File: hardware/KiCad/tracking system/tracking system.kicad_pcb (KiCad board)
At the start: 2 copper layers, 60 x 40 mm, 47 parts, among them J1 TP_SWD, J2 USB_C_Receptacle_PowerOnly_6P, J3 battery_conn, J5 GPS_Conn, J6 GSM_Conn, J7 OLED_conn, SW1 POWER_BTN, SW2 DIST_BTN, U1 STM32L476RETx, U2 TP4056-42-ESOP8, U3 ME6211C33M5, Y1 32kHz, Y2 8MHz

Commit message: work in progress
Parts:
- moved R7 79.8 mm to (129.0, 106.2)
- moved R8 79.6 mm to (129.0, 112.7)
- moved D1 63.4 mm to (154.5, 97.2), turned to 180 degrees
- moved C18 60.9 mm to (157.0, 112.0)
- moved C17 59.2 mm to (157.8, 107.0), turned to 180 degrees
- moved C19 57.7 mm to (159.7, 112.0), turned to 180 degrees
- moved R6 57.5 mm to (149.8, 102.8), turned to -90 degrees
- moved R5 50.6 mm to (158.0, 97.2)
- moved R9 49.5 mm to (160.5, 104.5), turned to -90 degrees
- moved C16 47.9 mm to (151.5, 107.0), turned to 180 degrees
- moved R4 44.3 mm to (163.0, 100.5), turned to -90 degrees
- moved R3 43.7 mm to (163.0, 98.2), turned to -90 degrees
- moved U2 3.26 mm to (155.2, 102.5)
- moved SW1 1.32 mm to (124.2, 107.2)
- moved SW2 1.32 mm to (124.2, 113.5)
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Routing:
- net +3.3V: track 0.00 -> 89.7 mm, vias 0 -> 2
- net GND: track 0.00 -> 78.5 mm, vias 0 -> 9
- net BTN_INT_EX2: track 0.00 -> 31.2 mm, vias 0 -> 4
- net BTN_PWR_EX3: track 0.00 -> 21.3 mm, vias 0 -> 2
- net RCC_OSC32_OUT: track 0.00 -> 19.2 mm, vias 0 -> 2
- net RCC_OSC_IN: track 0.00 -> 18.1 mm
- net RCC_OSC32_IN: track 0.00 -> 16.5 mm
- net USART3_RX: track 0.00 -> 14.5 mm
- net USART3_TX: track 0.00 -> 14.0 mm
- net /SWDIO: track 0.00 -> 12.8 mm
- net RCC_OSC_OUT: track 0.00 -> 12.2 mm
- net +3.3VA: track 0.00 -> 10.8 mm
- net /SWCLK: track 0.00 -> 7.93 mm
- net Net-(C12-Pad1): track 0.00 -> 4.70 mm
- net /NRST: track 0.00 -> 3.98 mm
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- added copper zone on F.Cu, net (none)
- added copper zone on B.Cu, net GND

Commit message: final pcb design
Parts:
- moved C3 1.75 mm to (135.5, 89.8)
- moved R2 1.75 mm to (137.8, 89.8)
- moved D1 0.25 mm to (154.8, 97.2)
- turned R5 to 180 degrees
- turned R6 to 90 degrees
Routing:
- net VBAT: track 0.00 -> 119.0 mm, vias 0 -> 6
- net +3.3V: track 89.7 -> 159.0 mm, vias 2 -> 4
- net GND: track 78.5 -> 126.4 mm, vias 9 -> 11
- net VBUS: track 0.00 -> 40.5 mm, vias 0 -> 2
- net USART1_TX: track 0.00 -> 22.5 mm
- net USART1_RX: track 0.00 -> 18.8 mm
- net I2C1_SDA: track 0.00 -> 14.5 mm
- net I2C1_SCL: track 0.00 -> 13.8 mm
- net Net-(U2-~{CHRG}): track 0.00 -> 6.99 mm, vias 0 -> 2
- net Net-(J2-CC1): track 0.00 -> 4.02 mm
- net Net-(J2-CC2): track 0.00 -> 3.92 mm
- net Net-(U2-PROG): track 0.00 -> 3.60 mm
- net Net-(U2-~{STDBY}): track 0.00 -> 3.13 mm
- net Net-(D1-K): track 0.00 -> 1.95 mm
- net /BOOT0: track 2.42 -> 3.54 mm
- removed copper zone on F.Cu, net (none)

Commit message: PCB done. About to send the files and start the firmware
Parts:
- added G***: LOGO, LOGO, F.Cu at (167.0, 90.2)
- moved H2 0.35 mm to (170.1, 117.4)
- moved H4 0.35 mm to (116.9, 117.4)
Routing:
- net GND: track 126.4 -> 127.9 mm, vias 11 -> 12
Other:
- outline, holes or cut-outs redrawn
- board text added: "MB-TRACK V1"

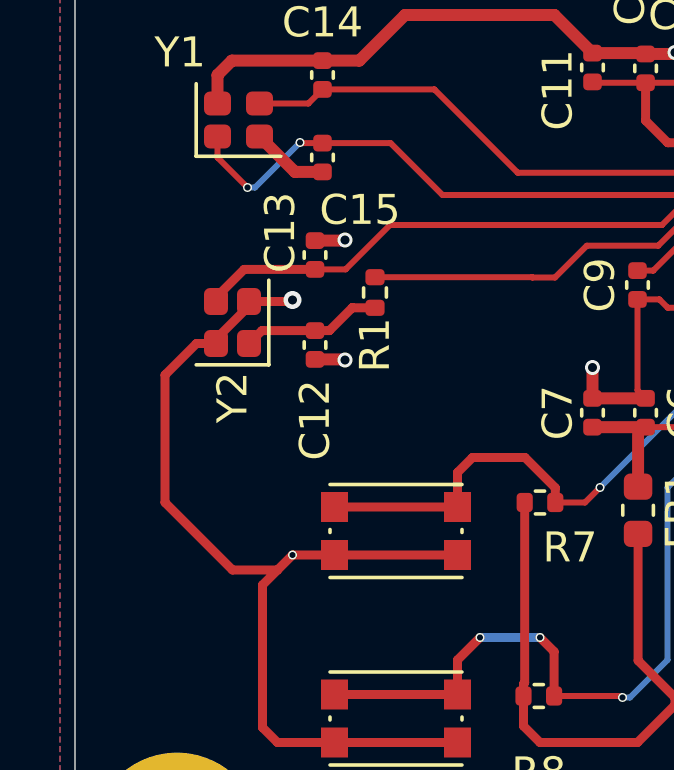
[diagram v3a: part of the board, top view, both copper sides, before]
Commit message: making changes to schematics and updating pcb
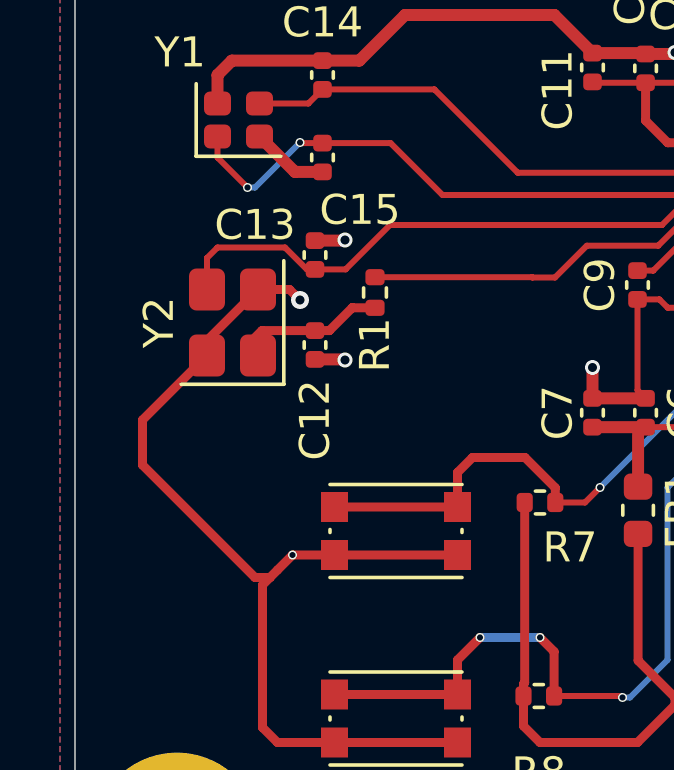
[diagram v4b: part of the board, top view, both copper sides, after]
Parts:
- Y2: footprint Crystal:Crystal_SMD_2016-4Pin_2.0x1.6mm -> Crystal:Crystal_SMD_3225-4Pin_3.2x2.5mm
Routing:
- net RCC_OSC_IN: track 18.1 -> 19.5 mm
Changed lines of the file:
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@@
 		(embedded_fonts no)
 	)
-	(footprint "Crystal:Crystal_SMD_2016-4Pin_2.0x1.6mm"
+	(footprint "Crystal:Crystal_SMD_3225-4Pin_3.2x2.5mm"
 		(layer "F.Cu")
 		(at 118.75 100.25 90)
-		(descr "SMD2016/4, Crystal, 2.0x1.6mm package, SMD, http://www.q-crystal.com/upload/5/2015552223166229.pdf")
+		(descr "SMD3225/4, Crystal, 3.2x2.5mm package, SMD, http://www.txccrystal.com/images/pdf/7m-accuracy.pdf")
 		(property "Reference" "Y2"
-			(at -2.5 0 90)
+			(at 0 -2.45 90)
 			(layer "F.SilkS")
 			(effects
@@
 		)
 		(property "Value" "8MHz"
-			(at 0 2 90)
+			(at 3 -3 90)
 			(layer "F.Fab")
 			(hide yes)
@@
 		(duplicate_pad_numbers_are_jumpers no)
 		(fp_line
-			(start -1.41 -1.21)
-			(end -1.41 1.21)
+			(start -2.06 -1.71)
+			(end -2.06 1.71)
 			(stroke
 				(width 0.12)
@@
 		)
 		(fp_line
-			(start -1.41 1.21)
-			(end 1.41 1.21)
+			(start -2.06 1.71)
+			(end 2.06 1.71)
 			(stroke
 				(width 0.12)
@@
 		)
 		(fp_rect
-			(start -1.5 -1.3)
-			(end 1.5 1.3)
+			(start -2.1 -1.75)
+			(end 2.1 1.75)
 			(stroke
 				(width 0.05)
@@
 		(fp_poly
 			(pts
-				(xy 1 -0.8) (xy 1 0.8) (xy -0.6 0.8) (xy -1 0.4) (xy -1 -0.8)
+				(xy 1.6 -1.25) (xy 1.6 1.25) (xy -0.975 1.25) (xy -1.6 0.625) (xy -1.6 -1.25)
 			)
 			(stroke
@@
 		)
 		(pad "1" smd roundrect
-			(at -0.7 0.55 90)
-			(size 0.9 0.8)
+			(at -1.1 0.85 90)
+			(size 1.4 1.2)
 			(layers "F.Cu" "F.Mask" "F.Paste")
-			(roundrect_rratio 0.25)
+			(roundrect_rratio 0.208333)
 			(net "Net-(C12-Pad1)")
 			(pinfunction "1_1")
@@
 		)
 		(pad "2" smd roundrect
-			(at 0.7 0.55 90)
-			(size 0.9 0.8)
+			(at 1.1 0.85 90)
+			(size 1.4 1.2)
 			(layers "F.Cu" "F.Mask" "F.Paste")
-			(roundrect_rratio 0.25)
+			(roundrect_rratio 0.208333)
 			(net "GND")
 			(pinfunction "G_2")
@@
 		)
 		(pad "3" smd roundrect
-			(at 0.7 -0.55 90)
-			(size 0.9 0.8)
+			(at 1.1 -0.85 90)
+			(size 1.4 1.2)
 			(layers "F.Cu" "F.Mask" "F.Paste")
-			(roundrect_rratio 0.25)
+			(roundrect_rratio 0.208333)
 			(net "RCC_OSC_IN")
 			(pinfunction "3_3")
@@
 		)
 		(pad "4" smd roundrect
-			(at -0.7 -0.55 90)
-			(size 0.9 0.8)
+			(at -1.1 -0.85 90)
+			(size 1.4 1.2)
 			(layers "F.Cu" "F.Mask" "F.Paste")
-			(roundrect_rratio 0.25)
+			(roundrect_rratio 0.208333)
 			(net "GND")
 			(pinfunction "G_4")
@@
 		)
 		(embedded_fonts no)
-		(model "${KICAD10_3DMODEL_DIR}/Crystal.3dshapes/Crystal_SMD_2016-4Pin_2.0x1.6mm.step"
+		(model "${KICAD10_3DMODEL_DIR}/Crystal.3dshapes/Crystal_SMD_3225-4Pin_3.2x2.5mm.step"
 			(offset
 				(xyz 0 0 0)
@@
 		(tags "capacitor")
 		(property "Reference" "C13"
-			(at 0.75 -1.16 90)
+			(at 1 -2 180)
 			(layer "F.SilkS")
 			(effects
@@
 	)
 	(segment
-		(start 147.319584 95.005575)
-		(end 147.336464 94.988695)
+		(start 115.75 103.5)
+		(end 115.75 105)
 		(width 0.3)
 		(layer "F.Cu")
@@
 	)
 	(segment
-		(start 119.3 99.55)
-		(end 119.3 99.7)
+		(start 147.319584 95.005575)
+		(end 147.336464 94.988695)
 		(width 0.3)
 		(layer "F.Cu")
@@
 	)
 	(segment
+		(start 119.5 108.75)
+		(end 120 108.75)
+		(width 0.3)
+		(layer "F.Cu")
+		(net "GND")
+	)
+	(segment
 		(start 137.269584 92.333695)
 		(end 137.269584 93.269584)
@@
 	)
 	(segment
-		(start 116.5 106.25)
-		(end 118.75 108.5)
-		(width 0.3)
-		(layer "F.Cu")
-		(net "GND")
-	)
-	(segment
 		(start 133.258695 99.758695)
 		(end 132.98 99.48)
@@
 	)
 	(segment
-		(start 119.3 99.55)
-		(end 120.7 99.55)
-		(width 0.3)
-		(layer "F.Cu")
-		(net "GND")
-	)
-	(segment
 		(start 142.75 111.5)
 		(end 143 111.75)
@@
 	)
 	(segment
-		(start 119.75 109)
+		(start 120 108.75)
 		(end 120.25 108.5)
 		(width 0.3)
@@
 	)
 	(segment
-		(start 119.3 99.7)
-		(end 118.2 100.8)
-		(width 0.3)
-		(layer "F.Cu")
-		(net "GND")
-	)
-	(segment
 		(start 164.25 102)
 		(end 166.92 102)
@@
 	)
 	(segment
-		(start 116.5 102)
-		(end 116.5 106.25)
+		(start 121.5 97.52)
+		(end 122.48 97.52)
+		(width 0.4)
+		(layer "F.Cu")
+		(net "GND")
+	)
+	(segment
+		(start 122.15 114.25)
+		(end 120.25 114.25)
 		(width 0.3)
 		(layer "F.Cu")
@@
 	)
 	(segment
-		(start 121.5 97.52)
-		(end 122.48 97.52)
+		(start 130.75 102.778695)
+		(end 130.75 101.75)
 		(width 0.4)
 		(layer "F.Cu")
@@
 	)
 	(segment
-		(start 118.2 100.95)
-		(end 117.55 100.95)
+		(start 119.6 99.15)
+		(end 120.65 99.15)
 		(width 0.3)
 		(layer "F.Cu")
@@
 	)
 	(segment
-		(start 122.15 114.25)
-		(end 120.25 114.25)
+		(start 119.75 109)
+		(end 120 108.75)
 		(width 0.3)
 		(layer "F.Cu")
@@
 	)
 	(segment
-		(start 130.75 102.778695)
-		(end 130.75 101.75)
-		(width 0.4)
+		(start 117.9 101.35)
+		(end 117.9 100.85)
+		(width 0.3)
+		(layer "F.Cu")
+		(net "GND")
+	)
+	(segment
+		(start 120.65 99.15)
+		(end 121 99.5)
+		(width 0.3)
 		(layer "F.Cu")
 		(net "GND")
@@
 	)
 	(segment
+		(start 117.9 101.35)
+		(end 115.75 103.5)
+		(width 0.3)
+		(layer "F.Cu")
+		(net "GND")
+	)
+	(segment
 		(start 120.25 108.5)
 		(end 120.75 108)
@@
 	)
 	(segment
+		(start 115.75 105)
+		(end 119.5 108.75)
+		(width 0.3)
+		(layer "F.Cu")
+		(net "GND")
+	)
+	(segment
 		(start 134.844584 99.758695)
 		(end 133.258695 99.758695)
@@
 	)
 	(segment
-		(start 118.75 108.5)
-		(end 120.25 108.5)
-		(width 0.3)
-		(layer "F.Cu")
-		(net "GND")
-	)
-	(segment
 		(start 132.490889 91.27)
 		(end 132.519584 91.298695)
@@
 	)
 	(segment
-		(start 118.2 100.8)
-		(end 118.2 100.95)
-		(width 0.3)
-		(layer "F.Cu")
-		(net "GND")
-	)
-	(segment
 		(start 154.615 103.135)
 		(end 155.25 102.5)
@@
 	)
 	(segment
-		(start 120.7 99.55)
-		(end 120.75 99.5)
-		(width 0.3)
-		(layer "F.Cu")
-		(net "GND")
-	)
-	(segment
 		(start 132.519584 102.778695)
 		(end 130.75 102.778695)
@@
 	)
 	(segment
-		(start 152.775 100.595)
-		(end 151.395 100.595)
-		(width 0.4)
+		(start 117.9 100.85)
+		(end 119.6 99.15)
+		(width 0.3)
 		(layer "F.Cu")
 		(net "GND")
 	)
 	(segment
-		(start 117.55 100.95)
-		(end 116.5 102)
-		(width 0.3)
+		(start 152.775 100.595)
+		(end 151.395 100.595)
+		(width 0.4)
 		(layer "F.Cu")
 		(net "GND")
@@
 	)
 	(via
-		(at 120.75 99.5)
-		(size 0.6)
-		(drill 0.3)
-		(layers "F.Cu" "B.Cu")
-		(net "GND")
-	)
-	(via
 		(at 151 111.25)
 		(size 0.5)
@@
 	)
 	(via
+		(at 121 99.5)
+		(size 0.6)
+		(drill 0.3)
+		(layers "F.Cu" "B.Cu")
+		(net "GND")
+	)
+	(via
 		(at 136.020416 89)
 		(size 0.5)
@@
 	)
 	(segment
-		(start 119.136642 98.48)
-		(end 118.2 99.416642)
-		(width 0.3)
+		(start 121.5 98.48)
+		(end 121.23 98.48)
+		(width 0.2)
 		(layer "F.Cu")
 		(net "RCC_OSC_IN")
@@
 	)
 	(segment
-		(start 121.5 98.48)
-		(end 119.136642 98.48)
-		(width 0.3)
+		(start 121.23 98.48)
+		(end 120.5 97.75)
+		(width 0.2)
+		(layer "F.Cu")
+		(net "RCC_OSC_IN")
+	)
+	(segment
+		(start 117.9 98.1)
+		(end 117.9 99.15)
+		(width 0.2)
 		(layer "F.Cu")
 		(net "RCC_OSC_IN")
@@
 	)
 	(segment
+		(start 118.25 97.75)
+		(end 117.9 98.1)
+		(width 0.2)
+		(layer "F.Cu")
+		(net "RCC_OSC_IN")
+	)
+	(segment
 		(start 133.806991 96.258695)
 		(end 133.065686 97)
 		(width 0.2)
 		(layer "F.Cu")
+		(net "RCC_OSC_IN")
+	)
+	(segment
+		(start 120.5 97.75)
+		(end 118.25 97.75)
+		(width 0.2)
+		(layer "F.Cu")

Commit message: crystal oscillator and ferrite bead change cause of BOM
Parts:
- removed Y1: 32kHz, Crystal:Crystal_SMD_2016-4Pin_2.0x1.6mm
- added Y3: 32kHz, Crystal:Crystal_SMD_3215-2Pin_3.2x1.5mm, F.Cu at (119.0, 93.5)
- C14, C15: value 10p -> 12.5p
- FB1: footprint Inductor_SMD:L_0603_1608Metric -> Inductor_SMD:L_0402_1005Metric
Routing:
- net GND: track 128.3 -> 122.0 mm, vias 12 -> 13
- net RCC_OSC32_OUT: track 19.2 -> 16.9 mm, vias 2 -> 0
- net RCC_OSC32_IN: track 16.5 -> 17.1 mm

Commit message: added manufacturer parts number for manufacturing
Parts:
- FB1: footprint Inductor_SMD:L_0402_1005Metric -> Inductor_SMD:L_0603_1608Metric
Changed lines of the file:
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@@
 		)
 	)
-	(footprint "Inductor_SMD:L_0402_1005Metric"
+	(footprint "Inductor_SMD:L_0603_1608Metric"
 		(layer "F.Cu")
 		(at 132.269584 106.508695 -90)
-		(descr "Inductor SMD 0402 (1005 Metric), square (rectangular) end terminal, IPC-7351 nominal, (Body size source: http://www.tortai-tech.com/upload/download/2011102023233369053.pdf)")
+		(descr "Inductor SMD 0603 (1608 Metric), square (rectangular) end terminal, IPC-7351 nominal, (Body size source: http://www.tortai-tech.com/upload/download/2011102023233369053.pdf)")
 		(tags "inductor")
 		(property "Reference" "FB1"
-			(at 0 -1.17 270)
+			(at 0 -1.43 270)
 			(layer "F.SilkS")
 			(effects
@@
 		)
 		(property "Value" "120R"
-			(at 0 1.17 270)
+			(at 0 1.43 270)
 			(layer "F.Fab")
-			(hide yes)
 			(effects
 				(font
@@
 		(attr smd)
 		(duplicate_pad_numbers_are_jumpers no)
+		(fp_line
+			(start -0.162779 0.51)
+			(end 0.162779 0.51)
+			(stroke
+				(width 0.12)
+				(type solid)
+			)
+			(layer "F.SilkS")
+		)
+		(fp_line
+			(start -0.162779 -0.51)
+			(end 0.162779 -0.51)
+			(stroke
+				(width 0.12)
+				(type solid)
+			)
+			(layer "F.SilkS")
+		)
 		(fp_rect
-			(start -0.93 -0.47)
-			(end 0.93 0.47)
+			(start -1.48 -0.73)
+			(end 1.48 0.73)
 			(stroke
 				(width 0.05)
@@
 		)
 		(fp_rect
-			(start -0.5 -0.25)
-			(end 0.5 0.25)
+			(start -0.8 -0.4)
+			(end 0.8 0.4)
 			(stroke
 				(width 0.1)
@@
 			(layer "F.Fab")
 		)
+		(fp_text user "${REFERENCE}"
+			(at 0 0 270)
+			(layer "F.Fab")
+			(effects
+				(font
+					(size 0.4 0.4)
+					(thickness 0.06)
+				)
+			)
+		)
 		(pad "1" smd roundrect
-			(at -0.485 0 270)
-			(size 0.59 0.64)
+			(at -0.7875 0 270)
+			(size 0.875 0.95)
 			(layers "F.Cu" "F.Mask" "F.Paste")
 			(roundrect_rratio 0.25)
@@
 		)
 		(pad "2" smd roundrect
-			(at 0.485 0 270)
-			(size 0.59 0.64)
+			(at 0.7875 0 270)
+			(size 0.875 0.95)
 			(layers "F.Cu" "F.Mask" "F.Paste")
 			(roundrect_rratio 0.25)
@@
 		)
 		(embedded_fonts no)
-		(model "${KICAD10_3DMODEL_DIR}/Inductor_SMD.3dshapes/L_0402_1005Metric.step"
+		(model "${KICAD10_3DMODEL_DIR}/Inductor_SMD.3dshapes/L_0603_1608Metric.step"
 			(offset
 				(xyz 0 0 0)
@@
 	)
 	(segment
-		(start 133.5 96)
-		(end 125.75 96)
-		(width 0.2)
-		(layer "F.Cu")
-		(net "RCC_OSC32_OUT")
-	)
-	(segment
-		(start 124.02 94.27)
-		(end 121.75 94.27)
-		(width 0.2)
-		(layer "F.Cu")
-		(net "RCC_OSC32_OUT")
-	)
-	(segment
-		(start 134.844584 95.758695)
-		(end 133.758695 95.758695)
-		(width 0.2)
-		(layer "F.Cu")
-		(net "RCC_OSC32_OUT")
-	)
-	(segment
-		(start 125.75 96)
-		(end 124.02 94.27)
-		(width 0.2)
-		(layer "F.Cu")
-		(net "RCC_OSC32_OUT")
-	)
-	(segment
-		(start 119 94.75)
-		(end 119.48 94.27)
-		(width 0.3)
-		(layer "F.Cu")
-		(net "RCC_OSC32_OUT")
-	)
-	(segment
-		(start 133.75 95.75)
-		(end 133.5 96)
-		(width 0.2)
-		(layer "F.Cu")
-		(net "RCC_OSC32_OUT")
-	)
-	(segment
-		(start 133.758695 95.758695)
-		(end 133.75 95.75)
-		(width 0.2)
-		(layer "F.Cu")
-		(net "RCC_OSC32_OUT")
-	)
-	(segment
-		(start 119.48 94.27)
-		(end 121.75 94.27)
-		(width 0.3)
-		(layer "F.Cu")
-		(net "RCC_OSC32_OUT")
-	)
-	(segment
-		(start 128.258695 95.258695)
-		(end 134.844584 95.258695)
-		(width 0.2)
-		(layer "F.Cu")
-		(net "RCC_OSC32_IN")
-	)
-	(segment
-		(start 125.48 92.48)
-		(end 128.258695 95.258695)
-		(width 0.2)
-		(layer "F.Cu")
-		(net "RCC_OSC32_IN")
-	)
-	(segment
-		(start 119 92.25)
-		(end 121.52 92.25)
-		(width 0.3)
-		(layer "F.Cu")
-		(net "RCC_OSC32_IN")
-	)
-	(segment
-		(start 121.75 92.48)
-		(end 125.48 92.48)
-		(width 0.2)
-		(layer "F.Cu")
-		(net "RCC_OSC32_IN")
-	)
-	(segment
-		(start 121.52 92.25)
-		(end 121.75 92.48)
-		(width 0.3)
-		(layer "F.Cu")
-		(net "RCC_OSC32_IN")
-	)
-	(segment
 		(start 166.68 99.99)
 		(end 166.92 99.75)
@@
 	)
 	(segment
+		(start 133.5 96)
+		(end 125.75 96)
+		(width 0.2)
+		(layer "F.Cu")
+		(net "RCC_OSC32_OUT")
+	)
+	(segment
+		(start 124.02 94.27)
+		(end 121.75 94.27)
+		(width 0.2)
+		(layer "F.Cu")
+		(net "RCC_OSC32_OUT")
+	)
+	(segment
+		(start 134.844584 95.758695)
+		(end 133.758695 95.758695)
+		(width 0.2)
+		(layer "F.Cu")
+		(net "RCC_OSC32_OUT")
+	)
+	(segment
+		(start 125.75 96)
+		(end 124.02 94.27)
+		(width 0.2)
+		(layer "F.Cu")
+		(net "RCC_OSC32_OUT")
+	)
+	(segment
+		(start 119 94.75)
+		(end 119.48 94.27)
+		(width 0.3)
+		(layer "F.Cu")
+		(net "RCC_OSC32_OUT")
+	)
+	(segment
+		(start 133.75 95.75)
+		(end 133.5 96)
+		(width 0.2)
+		(layer "F.Cu")
+		(net "RCC_OSC32_OUT")
+	)
+	(segment
+		(start 133.758695 95.758695)
+		(end 133.75 95.75)
+		(width 0.2)
+		(layer "F.Cu")
+		(net "RCC_OSC32_OUT")
+	)
+	(segment
+		(start 119.48 94.27)
+		(end 121.75 94.27)
+		(width 0.3)
+		(layer "F.Cu")
+		(net "RCC_OSC32_OUT")
+	)
+	(segment
 		(start 132.775869 98.52)
 		(end 134.037174 97.258695)
@@
 	)
 	(segment
+		(start 128.258695 95.258695)
+		(end 134.844584 95.258695)
+		(width 0.2)
+		(layer "F.Cu")
+		(net "RCC_OSC32_IN")
+	)
+	(segment
+		(start 125.48 92.48)
+		(end 128.258695 95.258695)
+		(width 0.2)
+		(layer "F.Cu")
+		(net "RCC_OSC32_IN")
+	)
+	(segment
+		(start 119 92.25)
+		(end 121.52 92.25)
+		(width 0.3)
+		(layer "F.Cu")
+		(net "RCC_OSC32_IN")
+	)
+	(segment
+		(start 121.75 92.48)
+		(end 125.48 92.48)
+		(width 0.2)
+		(layer "F.Cu")
+		(net "RCC_OSC32_IN")
+	)
+	(segment
+		(start 121.52 92.25)
+		(end 121.75 92.48)
+		(width 0.3)
+		(layer "F.Cu")
+		(net "RCC_OSC32_IN")
+	)
+	(segment

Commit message: Added more MPN, changed the load capacitance of the crystal from 12.5 to 12
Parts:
- C14, C15: value 12.5p -> 12p
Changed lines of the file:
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@@
 			)
 		)
-		(property "Value" "12.5p"
+		(property "Value" "12p"
 			(at 0 1.16 90)
 			(layer "F.Fab")
@@
 			)
 		)
-		(property "Value" "12.5p"
+		(property "Value" "12p"
 			(at 0 1.16 90)
 			(layer "F.Fab")
